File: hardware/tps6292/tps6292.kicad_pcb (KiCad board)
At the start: 2 copper layers, 17.5 x 38 mm, 17 parts, among them J1 Conn_01x02, J2 Conn_01x02, J3 Conn_01x02, J4 Conn_01x02, J5 Conn_01x02, U2 TPS629210DRLR, U4 BDR6133

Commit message: tps6292
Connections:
- J5 pad 1: GND -> VCC
- J5 pad 2: VCC -> GND
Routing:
- net VCC: track 33.5 -> 35.3 mm
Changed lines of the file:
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@@
 			(layers "F.Cu" "F.Mask" "F.Paste")
 			(roundrect_rratio 0.25)
-			(net 1 "GND")
+			(net 5 "VCC")
 			(pinfunction "Pin_1")
 			(pintype "passive")
@@
 			(layers "F.Cu" "F.Mask" "F.Paste")
 			(roundrect_rratio 0.25)
-			(net 5 "VCC")
+			(net 1 "GND")
 			(pinfunction "Pin_2")
 			(pintype "passive")
@@
 	)
 	(segment
+		(start 105.75 67)
+		(end 107.25 65.5)
+		(width 0.1524)
+		(layer "F.Cu")
+		(net 1)
+	)
+	(segment
 		(start 115.55 53.775)
 		(end 115.775 54)
@@
 	)
 	(segment
-		(start 104.25 67)
-		(end 104.25 64.25)
-		(width 0.1524)
-		(layer "F.Cu")
-		(net 1)
-	)
-	(segment
 		(start 115.55 52)
 		(end 115.55 52.5)
@@
 	)
 	(segment
+		(start 116 65.5)
+		(end 116.5 65.5)
+		(width 0.1524)
+		(layer "F.Cu")
+		(net 1)
+	)
+	(segment
 		(start 107.9 52)
 		(end 107.2 52.7)
@@
 	)
 	(via
-		(at 116 65.5)
-		(size 0.604799)
-		(drill 0.299999)
+		(at 109.4 56)
+		(size 0.8)
+		(drill 0.4)
 		(layers "F.Cu" "B.Cu")
 		(net 1)
 	)
 	(via
-		(at 109.4 56)
-		(size 0.8)
-		(drill 0.4)
+		(at 116.5 65.5)
+		(size 0.604799)
+		(drill 0.299999)
 		(layers "F.Cu" "B.Cu")
 		(net 1)
 	)
 	(via
-		(at 104.25 64.25)
+		(at 107.25 65.5)
 		(size 0.604799)
 		(drill 0.299999)
@@
 	)
 	(segment
-		(start 112.5 64.05)
-		(end 111.55 64.05)
+		(start 104.25 65.65)
+		(end 106.4 63.5)
 		(width 0.1524)
 		(layer "F.Cu")
@@
 	)
 	(segment
-		(start 112.5 64.5)
-		(end 113 65)
+		(start 112.5 64.05)
+		(end 111.55 64.05)
 		(width 0.1524)
 		(layer "F.Cu")
@@
 	)
 	(segment
-		(start 113 67)
-		(end 105.75 67)
+		(start 114.5 64)
+		(end 113.5 64)
 		(width 0.1524)
 		(layer "F.Cu")
@@
 	)
 	(segment
-		(start 113 65)
-		(end 113 67)
-		(width 0.1524)
-		(layer "F.Cu")
-		(net 5)
-	)
-	(segment
-		(start 112.5 64.05)
-		(end 112.5 64.5)
+		(start 113 67)
+		(end 113 64.55)
 		(width 0.1524)
 		(layer "F.Cu")
@@
 	)
 	(segment
-		(start 114.5 64)
-		(end 113.5 64)
+		(start 106.4 63.5)
+		(end 111 63.5)
 		(width 0.1524)
 		(layer "F.Cu")
@@
 	)
 	(segment
+		(start 113 64.55)
+		(end 112.5 64.05)
+		(width 0.1524)
+		(layer "F.Cu")
+		(net 5)
+	)
+	(segment
 		(start 115.85 62.15)
 		(end 116 62)
@@
 		(width 0.1524)
 		(layer "F.Cu")
+		(net 5)
+	)
+	(segment
+		(start 104.25 67)
+		(end 104.25 65.65)
+		(width 0.1524)
+		(layer "F.Cu")

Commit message: esp32
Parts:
- moved J3 0.50 mm to (105.5, 59.0)

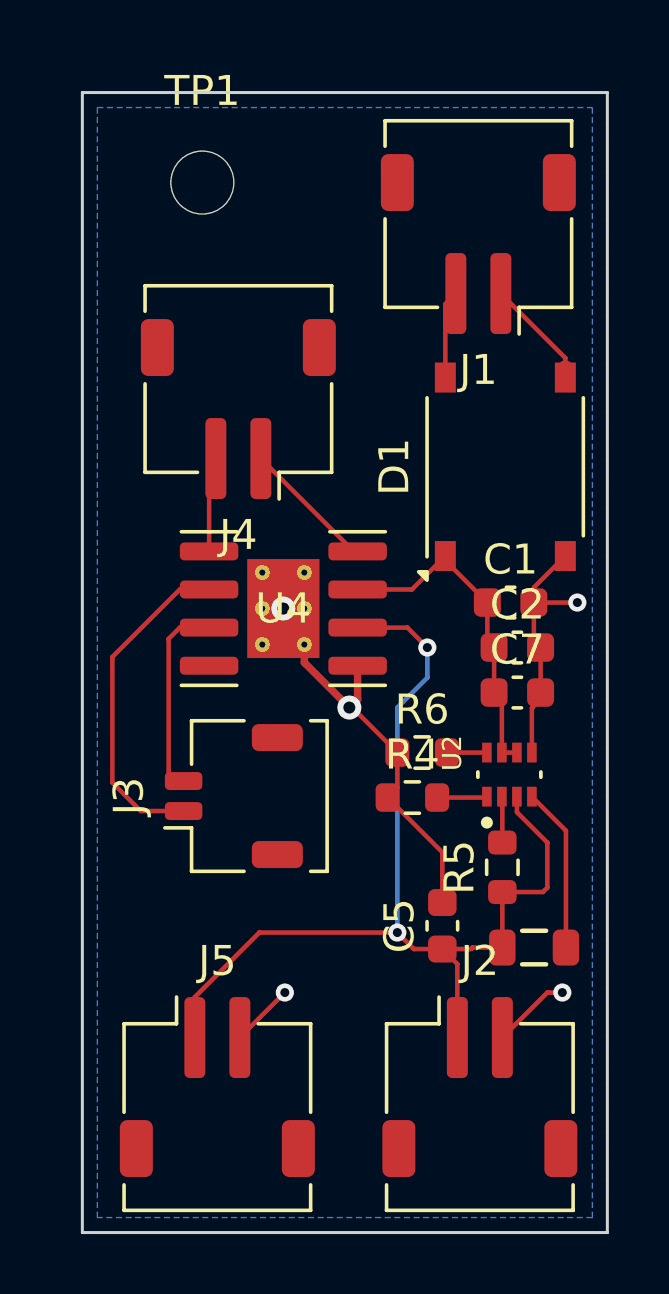
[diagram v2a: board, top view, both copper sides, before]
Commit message: power supply track sizes
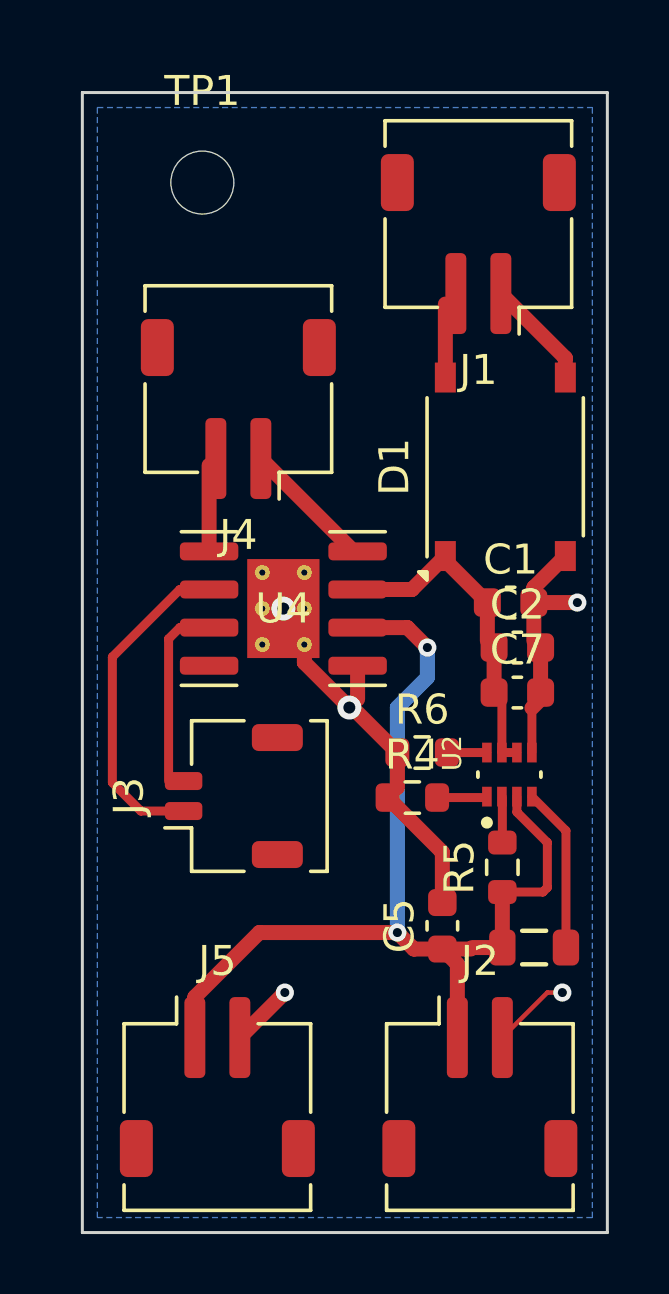
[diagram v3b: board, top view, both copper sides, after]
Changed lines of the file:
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@@
 		(start 111 57.5)
 		(end 111 58.675)
-		(width 0.1524)
+		(width 0.5)
 		(layer "F.Cu")
 		(net 1)
@@
 		(start 115.485 56.015)
 		(end 115.485 57.5)
-		(width 0.1524)
+		(width 0.3)
 		(layer "F.Cu")
 		(net 1)
@@
 		(start 105.75 67)
 		(end 107.25 65.5)
-		(width 0.1524)
+		(width 0.5)
 		(layer "F.Cu")
 		(net 1)
@@
 		(start 116.6 50.95)
 		(end 115.55 52)
-		(width 0.1524)
+		(width 0.5)
 		(layer "F.Cu")
 		(net 1)
@@
 		(start 107.9 54.5)
 		(end 109.4 56)
-		(width 0.25)
+		(width 0.5)
 		(layer "F.Cu")
 		(net 1)
@@
 		(start 115.55 52.5)
 		(end 115.55 53.775)
-		(width 0.1524)
+		(width 0.5)
 		(layer "F.Cu")
 		(net 1)
@@
 		(start 115.55 52)
 		(end 115.55 52.5)
-		(width 0.1524)
+		(width 0.5)
 		(layer "F.Cu")
 		(net 1)
@@
 		(start 115.775 55.725)
 		(end 115.485 56.015)
-		(width 0.1524)
+		(width 0.5)
 		(layer "F.Cu")
 		(net 1)
@@
 		(start 109.675 54.605)
 		(end 109.675 55.725)
-		(width 0.25)
+		(width 0.5)
 		(layer "F.Cu")
 		(net 1)
@@
 		(start 112.5 60.825)
 		(end 110.675 59)
-		(width 0.1524)
+		(width 0.5)
 		(layer "F.Cu")
 		(net 1)
@@
 		(start 112.5 62.5)
 		(end 112.5 60.825)
-		(width 0.1524)
+		(width 0.5)
 		(layer "F.Cu")
 		(net 1)
@@
 		(start 111 57.5)
 		(end 109.5 56)
-		(width 0.1524)
+		(width 0.5)
 		(layer "F.Cu")
 		(net 1)
@@
 		(start 115.55 52.5)
 		(end 117 52.5)
-		(width 0.1524)
+		(width 0.5)
 		(layer "F.Cu")
 		(net 1)
@@
 		(start 115.775 54)
 		(end 115.775 55.5)
-		(width 0.1524)
+		(width 0.5)
 		(layer "F.Cu")
 		(net 1)
@@
 		(start 107.9 53.9)
 		(end 107.9 54.5)
-		(width 0.25)
+		(width 0.5)
 		(layer "F.Cu")
 		(net 1)
@@
 		(start 114 52.5)
 		(end 114 53.775)
-		(width 0.1524)
+		(width 0.5)
 		(layer "F.Cu")
 		(net 2)
@@
 		(start 114.985 57.5)
 		(end 114.485 57.5)
-		(width 0.1524)
+		(width 0.3)
 		(layer "F.Cu")
 		(net 2)
@@
 		(start 111.485 52.065)
 		(end 112.6 50.95)
-		(width 0.1524)
+		(width 0.5)
 		(layer "F.Cu")
 		(net 2)
@@
 		(start 109.675 52.065)
 		(end 111.485 52.065)
-		(width 0.1524)
+		(width 0.5)
 		(layer "F.Cu")
 		(net 2)
@@
 		(start 114.485 55.76)
 		(end 114.485 57.5)
-		(width 0.1524)
+		(width 0.3)
 		(layer "F.Cu")
 		(net 2)
@@
 		(start 112.6 51.1)
 		(end 114 52.5)
-		(width 0.1524)
+		(width 0.5)
 		(layer "F.Cu")
 		(net 2)
@@
 		(start 114.225 54)
 		(end 114.225 55.5)
-		(width 0.1524)
+		(width 0.5)
 		(layer "F.Cu")
 		(net 2)
@@
 		(start 112.6 45)
 		(end 112.6 42.55)
-		(width 0.1524)
+		(width 0.5)
 		(layer "F.Cu")
 		(net 3)
@@
 		(start 116.6 44.35)
 		(end 114.45 42.2)
-		(width 0.1524)
+		(width 0.5)
 		(layer "F.Cu")
 		(net 4)
@@
 		(start 116.6 45)
 		(end 116.6 44.35)
-		(width 0.1524)
+		(width 0.5)
 		(layer "F.Cu")
 		(net 4)
@@
 		(start 104.25 65.65)
 		(end 106.4 63.5)
-		(width 0.1524)
+		(width 0.5)
 		(layer "F.Cu")
 		(net 5)
@@
 		(start 112.5 64.05)
 		(end 111.55 64.05)
-		(width 0.1524)
+		(width 0.5)
 		(layer "F.Cu")
 		(net 5)
@@
 		(start 113.45 64.05)
 		(end 112.5 64.05)
-		(width 0.1524)
+		(width 0.5)
 		(layer "F.Cu")
 		(net 5)
@@
 		(start 116 60.5)
 		(end 114.985 59.485)
-		(width 0.1524)
+		(width 0.3)
 		(layer "F.Cu")
 		(net 5)
@@
 		(start 114.5 64)
 		(end 113.5 64)
-		(width 0.1524)
+		(width 0.5)
 		(layer "F.Cu")
 		(net 5)
@@
 		(start 109.675 53.335)
 		(end 111.335 53.335)
-		(width 0.1524)
+		(width 0.5)
 		(layer "F.Cu")
 		(net 5)
@@
 		(start 113 67)
 		(end 113 64.55)
-		(width 0.1524)
+		(width 0.5)
 		(layer "F.Cu")
 		(net 5)
@@
 		(start 114.5 62.15)
 		(end 115.85 62.15)
-		(width 0.1524)
+		(width 0.3)
 		(layer "F.Cu")
 		(net 5)
@@
 		(start 106.4 63.5)
 		(end 111 63.5)
-		(width 0.1524)
+		(width 0.5)
 		(layer "F.Cu")
 		(net 5)
@@
 		(start 114.5 64)
 		(end 114.5 62.15)
-		(width 0.1524)
+		(width 0.5)
 		(layer "F.Cu")
 		(net 5)
@@
 		(start 111.55 64.05)
 		(end 111 63.5)
-		(width 0.1524)
+		(width 0.5)
 		(layer "F.Cu")
 		(net 5)
@@
 		(start 114.985 59.485)
 		(end 114.985 58.97)
-		(width 0.1524)
+		(width 0.3)
 		(layer "F.Cu")
 		(net 5)
@@
 		(start 113 64.55)
 		(end 112.5 64.05)
-		(width 0.1524)
+		(width 0.5)
 		(layer "F.Cu")
 		(net 5)
@@
 		(start 115.85 62.15)
 		(end 116 62)
-		(width 0.1524)
+		(width 0.3)
 		(layer "F.Cu")
 		(net 5)
@@
 		(start 111.335 53.335)
 		(end 112 54)
-		(width 0.1524)
+		(width 0.5)
 		(layer "F.Cu")
 		(net 5)
@@
 		(start 104.25 67)
 		(end 104.25 65.65)
-		(width 0.1524)
+		(width 0.5)
 		(layer "F.Cu")
 		(net 5)
@@
 		(start 116 62)
 		(end 116 60.5)
-		(width 0.1524)
+		(width 0.3)
 		(layer "F.Cu")
 		(net 5)
@@
 		(start 112 55)
 		(end 111 56)
-		(width 0.1524)
+		(width 0.5)
 		(layer "B.Cu")
 		(net 5)
@@
 		(start 111 56)
 		(end 111 63.5)
-		(width 0.1524)
+		(width 0.5)
 		(layer "B.Cu")
 		(net 5)
@@
 		(start 112 54)
 		(end 112 55)
-		(width 0.1524)
+		(width 0.5)
 		(layer "B.Cu")
 		(net 5)
@@
 		(start 109.545 50.795)
 		(end 106.45 47.7)
-		(width 0.1524)
+		(width 0.5)
 		(layer "F.Cu")
 		(net 6)
@@
 		(start 104.725 50.795)
 		(end 104.725 47.925)
-		(width 0.1524)
+		(width 0.5)
 		(layer "F.Cu")
 		(net 7)
@@
 		(start 103.375 59.45)
 		(end 102.45 59.45)
-		(width 0.1524)
+		(width 0.3)
 		(layer "F.Cu")
 		(net 9)
@@
 		(start 102.45 59.45)
 		(end 101.5 58.5)
-		(width 0.1524)
+		(width 0.3)
 		(layer "F.Cu")
 		(net 9)
@@
 		(start 101.5 58.5)
 		(end 101.5 54.315001)
-		(width 0.1524)
+		(width 0.3)
 		(layer "F.Cu")
 		(net 9)
@@
 		(start 101.5 54.315001)
 		(end 103.750001 52.065)
-		(width 0.1524)
+		(width 0.3)
 		(layer "F.Cu")
 		(net 9)
@@
 		(start 103.750001 52.065)
 		(end 104.725 52.065)
-		(width 0.1524)
+		(width 0.3)
 		(layer "F.Cu")
 		(net 9)
@@
 		(start 104.725 53.335)
 		(end 103.750001 53.335)
-		(width 0.1524)
+		(width 0.3)
 		(layer "F.Cu")
 		(net 10)
@@
 		(start 103.375 53.710001)
 		(end 103.375 58.45)
-		(width 0.1524)
+		(width 0.3)
 		(layer "F.Cu")
 		(net 10)
@@
 		(start 103.750001 53.335)
 		(end 103.375 53.710001)
-		(width 0.1524)
+		(width 0.3)
 		(layer "F.Cu")
 		(net 10)
@@
 		(start 116.62 60.105)
 		(end 115.485 58.97)
-		(width 0.1524)
+		(width 0.3)
 		(layer "F.Cu")
 		(net 11)
@@
 		(start 116.62 64)
 		(end 116.62 60.105)
-		(width 0.1524)
+		(width 0.3)
 		(layer "F.Cu")
 		(net 11)
@@
 		(start 112.325 59)
 		(end 113.955 59)
-		(width 0.1524)
+		(width 0.3)
 		(layer "F.Cu")
 		(net 12)
@@
 		(start 114.5 60.5)
 		(end 114.5 58.985)
-		(width 0.1524)
+		(width 0.3)
 		(layer "F.Cu")
 		(net 13)
@@
 		(start 113.985 57.5)
 		(end 112.65 57.5)
-		(width 0.1524)
+		(width 0.3)
 		(layer "F.Cu")
 		(net 14)

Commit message: some fixes
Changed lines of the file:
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@@
 		(start 114.5 67)
 		(end 116 65.5)
-		(width 0.1524)
+		(width 0.5)
 		(layer "F.Cu")
 		(net 1)
@@
 		(start 116 65.5)
 		(end 116.5 65.5)
-		(width 0.1524)
+		(width 0.5)
 		(layer "F.Cu")
 		(net 1)

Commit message: adjustments
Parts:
- added TP2: TestPoint, TestPoint:TestPoint_Pad_1.0x1.0mm, F.Cu at (104.5, 37.5)
- added TP3: TestPoint, TestPoint:TestPoint_Pad_1.0x1.0mm, F.Cu at (106.5, 37.5)
- added TP4: TestPoint, TestPoint:TestPoint_Pad_1.0x1.0mm, F.Cu at (108.5, 37.5)
- TP1: footprint MountingHole:MountingHole_2.1mm -> TestPoint:TestPoint_Pad_1.0x1.0mm
- moved TP1 2.37 mm to (102.3, 37.5), turned to 90 degrees
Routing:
- net GND: track 33.1 -> 41.2 mm, vias 5 -> 6

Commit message: jlcpcb wip
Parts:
- removed TP1, TP2, TP3, TP4: TestPoint, TestPoint:TestPoint_Pad_1.0x1.0mm
- added J6: Conn_01x01, Connector_PinHeader_1.00mm:PinHeader_1x01_P1.00mm_Vertical, F.Cu at (102.4, 38.0)
- added J7: Conn_01x01, Connector_PinHeader_1.00mm:PinHeader_1x01_P1.00mm_Vertical, F.Cu at (105.5, 38.0)
- added J8: Conn_01x01, Connector_PinHeader_1.00mm:PinHeader_1x01_P1.00mm_Vertical, F.Cu at (108.5, 38.0)

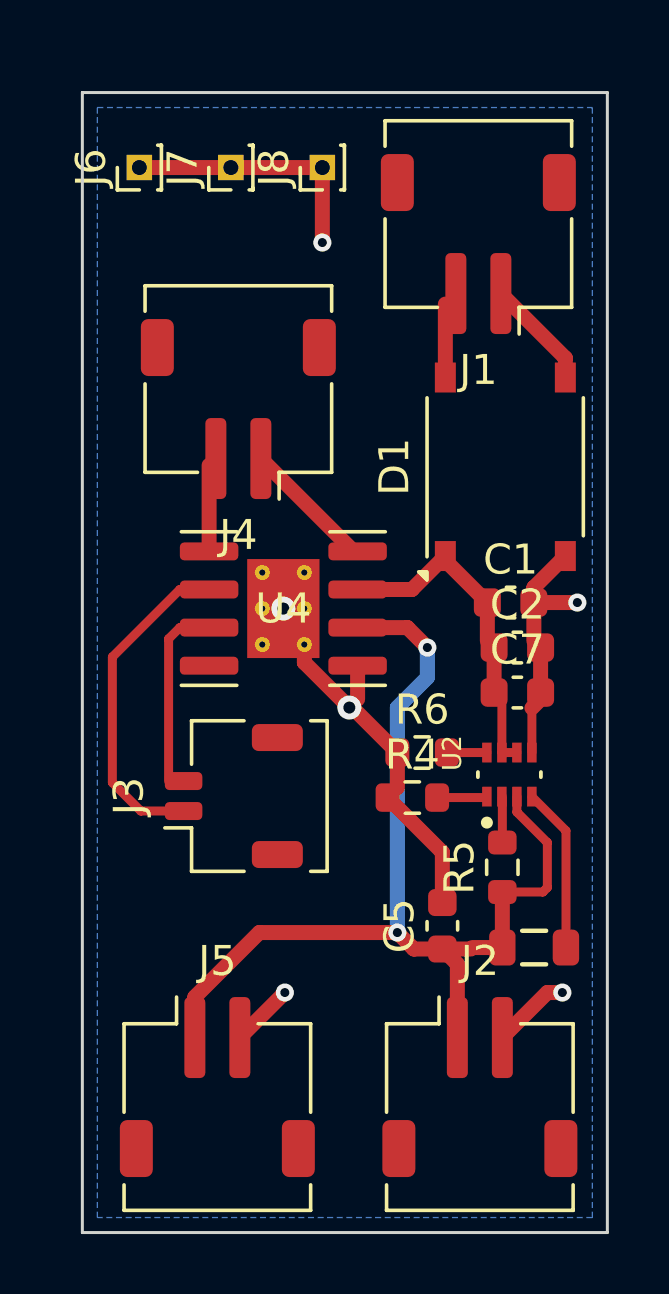
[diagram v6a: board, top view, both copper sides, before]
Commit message: replace connectors
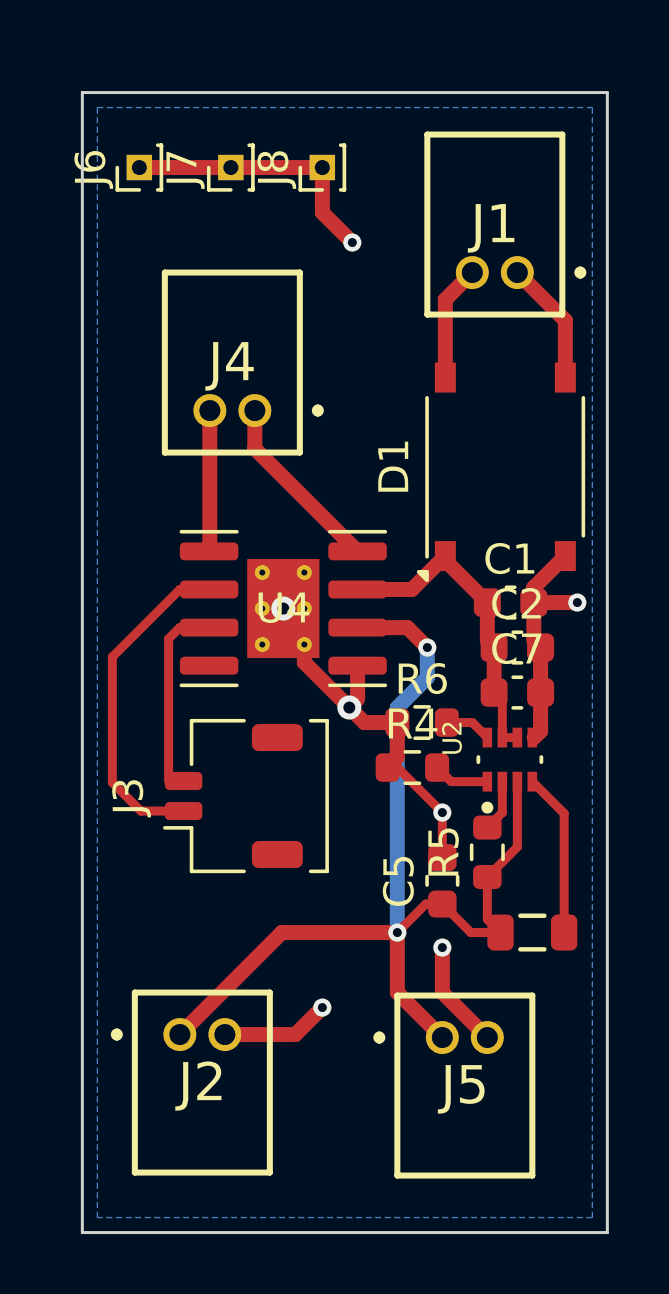
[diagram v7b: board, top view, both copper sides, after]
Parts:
- J1, J2, J4, J5: footprint Connector_JST:JST_ZH_S2B-ZR-SM4A-TF_1x02-1MP_P1.50mm_Horizontal -> LIB_S2B-ZR_LF__SN_:S2BZRLFSN
- moved J2 10.2 mm to (103.8, 66.9)
- moved J5 7.68 mm to (112.5, 67.0)
- moved J1 1.61 mm to (115.0, 41.5)
- moved C5 1.50 mm to (112.5, 61.8)
- moved R4 1.00 mm to (111.5, 58.0)
- moved R6 1.00 mm to (111.8, 56.5)
- moved R5 0.71 mm to (114.0, 60.8)
- moved J4 0.55 mm to (106.2, 46.1)
- moved L1 0.50 mm to (115.5, 63.5)
- moved U2 0.50 mm to (114.8, 57.7)
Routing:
- net GND: track 41.7 -> 43.5 mm, vias 6 -> 7
- net Net-(J4-Pin_1): track 4.51 -> 6.11 mm
- net Net-(J4-Pin_2): track 3.19 -> 4.71 mm
- net Net-(J1-Pin_2): track 2.94 -> 3.87 mm
